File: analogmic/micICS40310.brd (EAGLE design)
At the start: 8.9 x 18.9 mm, 4 parts

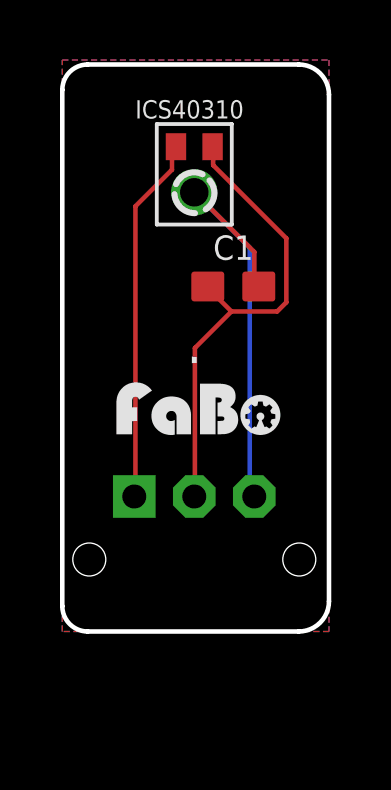
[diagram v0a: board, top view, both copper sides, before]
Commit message: Update opamp.
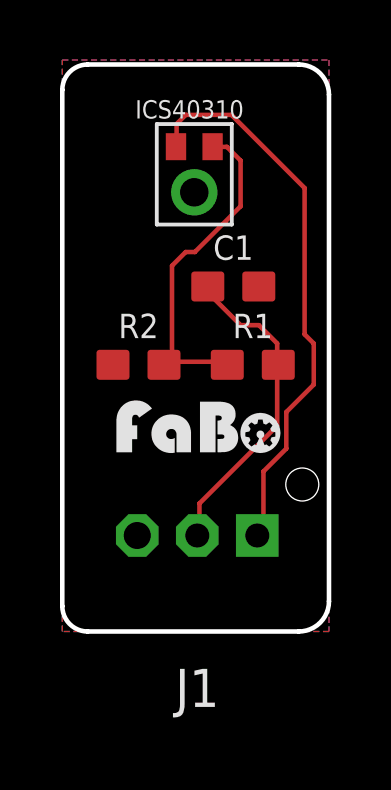
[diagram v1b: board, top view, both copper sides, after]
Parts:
- removed .: (no value), FaBo-Template:FABO_BRICK_3PIN_S03B-PASK-2
- added J1: (no value), FaBo-Template:FABO_BRICK_3PIN_B03B-PASK-1_NAME_BOTTOM
- added R1: 2K, FaBo-Resistors:0603
- added R2: 1K, FaBo-Resistors:0603
- moved U$2 0.60 mm to (4.60, 5.80)
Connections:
- new net N$1: ICS40310.3, R1.1, R2.2
- net 3V3: now also J1.VCC, R1.2; no longer ..VCC, ICS40310.3
- net GND: now also J1.GND, R2.1; no longer ..GND
- net OUTPUT: now also J1.I/O; no longer ..I/O
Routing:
- net GND: track 15.1 -> 0.00 mm
- net N$1: track 0.00 -> 11.3 mm
- net OUTPUT: track 12.3 -> 18.7 mm
- net 3V3: track 16.0 -> 10.9 mm
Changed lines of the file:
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@@
 <setting verticaltext="up"/>
 </settings>
-<grid distance="1.27" unitdist="mm" unit="mm" style="lines" multiple="1" display="yes" altdistance="5" altunitdist="mil" altunit="mil"/>
+<grid distance="0.1" unitdist="mm" unit="mm" style="lines" multiple="1" display="yes" altdistance="5" altunitdist="mil" altunit="mil"/>
 <layers>
 <layer number="1" name="Top" color="4" fill="1" visible="yes" active="yes"/>
@@
 <layer number="25" name="tNames" color="7" fill="1" visible="yes" active="yes"/>
 <layer number="26" name="bNames" color="7" fill="1" visible="yes" active="yes"/>
-<layer number="27" name="tValues" color="7" fill="1" visible="yes" active="yes"/>
+<layer number="27" name="tValues" color="7" fill="1" visible="no" active="yes"/>
 <layer number="28" name="bValues" color="7" fill="1" visible="yes" active="yes"/>
 <layer number="29" name="tStop" color="7" fill="3" visible="no" active="yes"/>
@@
 <attribute name="VALUE" x="5.7" y="11.5" size="0.8128" layer="27" font="vector" ratio="12" align="center"/>
 </element>
-<element name="." library="FaBo-Template" package="FABO_BRICK_3PIN_S03B-PASK-2" value="" x="4.4" y="4.5" smashed="yes" rot="R180">
-<attribute name="NAME" x="4.4" y="8.945" size="1.27" layer="25" font="vector" ratio="12" align="bottom-center"/>
-</element>
-<element name="U$2" library="FaBo-Logo" package="LOGO_FABO_S" value="" x="4.6" y="6.4" smashed="yes"/>
+<element name="U$2" library="FaBo-Logo" package="LOGO_FABO_S" value="" x="4.6" y="5.8" smashed="yes"/>
 <element name="ICS40310" library="FaBo-Sound" package="ICS40310" value="ANALOG-MICICS40310" x="4.4" y="15.24" smashed="yes">
 <attribute name="NAME" x="4.24" y="17.1" size="0.6096" layer="25" align="bottom-center"/>
+</element>
+<element name="R1" library="FaBo-Resistors" package="0603" value="2K" x="6.35" y="8.89" smashed="yes">
+<attribute name="NAME" x="6.35" y="9.779" size="0.8128" layer="25" font="vector" ratio="12" align="bottom-center"/>
+<attribute name="VALUE" x="6.35" y="8.89" size="0.8128" layer="27" font="vector" ratio="12" align="center"/>
+</element>
+<element name="R2" library="FaBo-Resistors" package="0603" value="1K" x="2.54" y="8.89" smashed="yes">
+<attribute name="NAME" x="2.54" y="9.779" size="0.8128" layer="25" font="vector" ratio="12" align="bottom-center"/>
+<attribute name="VALUE" x="2.54" y="8.89" size="0.8128" layer="27" font="vector" ratio="12" align="center"/>
+</element>
+<element name="J1" library="FaBo-Template" package="FABO_BRICK_3PIN_B03B-PASK-1_NAME_BOTTOM" value="" x="4.5" y="3.2" smashed="yes">
+<attribute name="NAME" x="4.5" y="-2.515" size="1.27" layer="25" font="vector" ratio="12" align="bottom-center"/>
 </element>
 </elements>
@@
 <signal name="GND">
 <contactref element="C1" pad="2"/>
-<contactref element="." pad="GND"/>
 <contactref element="ICS40310" pad="2"/>
-<wire x1="6.4008" y1="12.6492" x2="6.4008" y2="11.5824" width="0.1524" layer="1"/>
-<wire x1="4.4196" y1="14.6304" x2="6.4008" y2="12.6492" width="0.1524" layer="1"/>
-<wire x1="6.4008" y1="11.5824" x2="6.55" y2="11.5" width="0.1524" layer="1"/>
-<wire x1="4.4196" y1="14.6304" x2="4.4" y2="14.64" width="0.1524" layer="1"/>
-<wire x1="6.2484" y1="12.8016" x2="6.2484" y2="4.572" width="0.1524" layer="16"/>
-<wire x1="4.4196" y1="14.6304" x2="6.2484" y2="12.8016" width="0.1524" layer="16"/>
-<wire x1="6.2484" y1="4.572" x2="6.4" y2="4.5" width="0.1524" layer="16"/>
-<wire x1="4.4196" y1="14.6304" x2="4.4" y2="14.64" width="0.1524" layer="16"/>
 <polygon width="0.1524" layer="16">
 <vertex x="0" y="0"/>
@@
 <vertex x="8.89" y="0"/>
 </polygon>
+<contactref element="R2" pad="1"/>
+<contactref element="J1" pad="GND"/>
 </signal>
 <signal name="OUTPUT">
-<contactref element="." pad="I/O"/>
 <contactref element="ICS40310" pad="1"/>
-<wire x1="3.6576" y1="15.3924" x2="3.6576" y2="16.1544" width="0.1524" layer="1"/>
-<wire x1="2.4384" y1="14.1732" x2="3.6576" y2="15.3924" width="0.1524" layer="1"/>
-<wire x1="2.4384" y1="4.572" x2="2.4384" y2="14.1732" width="0.1524" layer="1"/>
-<wire x1="3.6576" y1="16.1544" x2="3.79" y2="16.16" width="0.1524" layer="1"/>
-<wire x1="2.4384" y1="4.572" x2="2.4" y2="4.5" width="0.1524" layer="1"/>
+<contactref element="J1" pad="I/O"/>
+<wire x1="3.81" y1="16.9164" x2="3.81" y2="16.3068" width="0.1524" layer="1"/>
+<wire x1="4.1148" y1="17.2212" x2="3.81" y2="16.9164" width="0.1524" layer="1"/>
+<wire x1="5.6388" y1="17.2212" x2="4.1148" y2="17.2212" width="0.1524" layer="1"/>
+<wire x1="8.0772" y1="14.7828" x2="5.6388" y2="17.2212" width="0.1524" layer="1"/>
+<wire x1="8.0772" y1="9.906" x2="8.0772" y2="14.7828" width="0.1524" layer="1"/>
+<wire x1="8.382" y1="9.6012" x2="8.0772" y2="9.906" width="0.1524" layer="1"/>
+<wire x1="8.382" y1="8.2296" x2="8.382" y2="9.6012" width="0.1524" layer="1"/>
+<wire x1="7.4676" y1="7.3152" x2="8.382" y2="8.2296" width="0.1524" layer="1"/>
+<wire x1="7.4676" y1="6.096" x2="7.4676" y2="7.3152" width="0.1524" layer="1"/>
+<wire x1="6.7056" y1="5.334" x2="7.4676" y2="6.096" width="0.1524" layer="1"/>
+<wire x1="6.7056" y1="3.3528" x2="6.7056" y2="5.334" width="0.1524" layer="1"/>
+<wire x1="6.5532" y1="3.2004" x2="6.7056" y2="3.3528" width="0.1524" layer="1"/>
+<wire x1="3.81" y1="16.3068" x2="3.79" y2="16.16" width="0.1524" layer="1"/>
+<wire x1="6.5532" y1="3.2004" x2="6.5" y2="3.2" width="0.1524" layer="1"/>
 </signal>
 <signal name="3V3">
 <contactref element="C1" pad="1"/>
-<contactref element="." pad="VCC"/>
+<contactref element="R1" pad="2"/>
+<contactref element="J1" pad="VCC"/>
+<wire x1="7.1628" y1="9.6012" x2="7.1628" y2="8.9916" width="0.1524" layer="1"/>
+<wire x1="6.5532" y1="10.2108" x2="7.1628" y2="9.6012" width="0.1524" layer="1"/>
+<wire x1="5.9436" y1="10.2108" x2="6.5532" y2="10.2108" width="0.1524" layer="1"/>
+<wire x1="4.7244" y1="11.43" x2="5.9436" y2="10.2108" width="0.1524" layer="1"/>
+<wire x1="7.1628" y1="8.9916" x2="7.2" y2="8.89" width="0.1524" layer="1"/>
+<wire x1="4.7244" y1="11.43" x2="4.85" y2="11.5" width="0.1524" layer="1"/>
+<wire x1="7.1628" y1="6.858" x2="7.1628" y2="8.8392" width="0.1524" layer="1"/>
+<wire x1="4.572" y1="4.2672" x2="7.1628" y2="6.858" width="0.1524" layer="1"/>
+<wire x1="4.572" y1="3.2004" x2="4.572" y2="4.2672" width="0.1524" layer="1"/>
+<wire x1="7.1628" y1="8.8392" x2="7.2" y2="8.89" width="0.1524" layer="1"/>
+<wire x1="4.572" y1="3.2004" x2="4.5" y2="3.2" width="0.1524" layer="1"/>
+</signal>
+<signal name="N$1">
+<contactref element="R1" pad="1"/>
+<contactref element="R2" pad="2"/>
 <contactref element="ICS40310" pad="3"/>
-<wire x1="5.0292" y1="15.5448" x2="5.0292" y2="16.1544" width="0.1524" layer="1"/>
-<wire x1="7.4676" y1="13.1064" x2="5.0292" y2="15.5448" width="0.1524" layer="1"/>
-<wire x1="7.4676" y1="10.9728" x2="7.4676" y2="13.1064" width="0.1524" layer="1"/>
-<wire x1="7.1628" y1="10.668" x2="7.4676" y2="10.9728" width="0.1524" layer="1"/>
-<wire x1="5.6388" y1="10.668" x2="7.1628" y2="10.668" width="0.1524" layer="1"/>
-<wire x1="4.8768" y1="11.43" x2="5.6388" y2="10.668" width="0.1524" layer="1"/>
+<wire x1="5.4864" y1="16.1544" x2="5.0292" y2="16.1544" width="0.1524" layer="1"/>
+<wire x1="5.9436" y1="15.6972" x2="5.4864" y2="16.1544" width="0.1524" layer="1"/>
+<wire x1="5.9436" y1="14.1732" x2="5.9436" y2="15.6972" width="0.1524" layer="1"/>
+<wire x1="4.4196" y1="12.6492" x2="5.9436" y2="14.1732" width="0.1524" layer="1"/>
+<wire x1="4.1148" y1="12.6492" x2="4.4196" y2="12.6492" width="0.1524" layer="1"/>
+<wire x1="3.6576" y1="12.192" x2="4.1148" y2="12.6492" width="0.1524" layer="1"/>
+<wire x1="3.6576" y1="9.144" x2="3.6576" y2="12.192" width="0.1524" layer="1"/>
+<wire x1="3.5052" y1="8.9916" x2="3.6576" y2="9.144" width="0.1524" layer="1"/>
 <wire x1="5.0292" y1="16.1544" x2="5.01" y2="16.16" width="0.1524" layer="1"/>
-<wire x1="4.8768" y1="11.43" x2="4.85" y2="11.5" width="0.1524" layer="1"/>
-<wire x1="4.4196" y1="9.4488" x2="4.4196" y2="4.572" width="0.1524" layer="1"/>
-<wire x1="5.6388" y1="10.668" x2="4.4196" y2="9.4488" width="0.1524" layer="1"/>
-<wire x1="4.4196" y1="4.572" x2="4.4" y2="4.5" width="0.1524" layer="1"/>
+<wire x1="3.5052" y1="8.9916" x2="5.4864" y2="8.9916" width="0.1524" layer="1"/>
+<wire x1="5.4864" y1="8.9916" x2="5.5" y2="8.89" width="0.1524" layer="1"/>
+<wire x1="3.5052" y1="8.9916" x2="3.39" y2="8.89" width="0.1524" layer="1"/>
 </signal>
 </signals>
